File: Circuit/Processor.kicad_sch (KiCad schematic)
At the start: 22 parts, among them J6 Conn_01x03_Pin, J7 Conn_01x02_Pin, J8 Conn_01x02_Pin, U1 STM32G491CCUx, Y1 ECS-2520MV-xxx-xx

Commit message: Output job, Revision Box and reorganise
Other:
- company: Harry and Yuki - EEE3 Instrumentation -> Harry Hill and Yuki Hoshino
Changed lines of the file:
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@@
 	(title_block
 		(title "Processor")
-		(date "2026-03-02")
+		(date "2026-05-02")
 		(rev "1.0")
-		(company "Harry and Yuki - EEE3 Instrumentation")
+		(company "Harry Hill and Yuki Hoshino")
+		(comment 1 "LCR Meter")
 	)
 	(junction

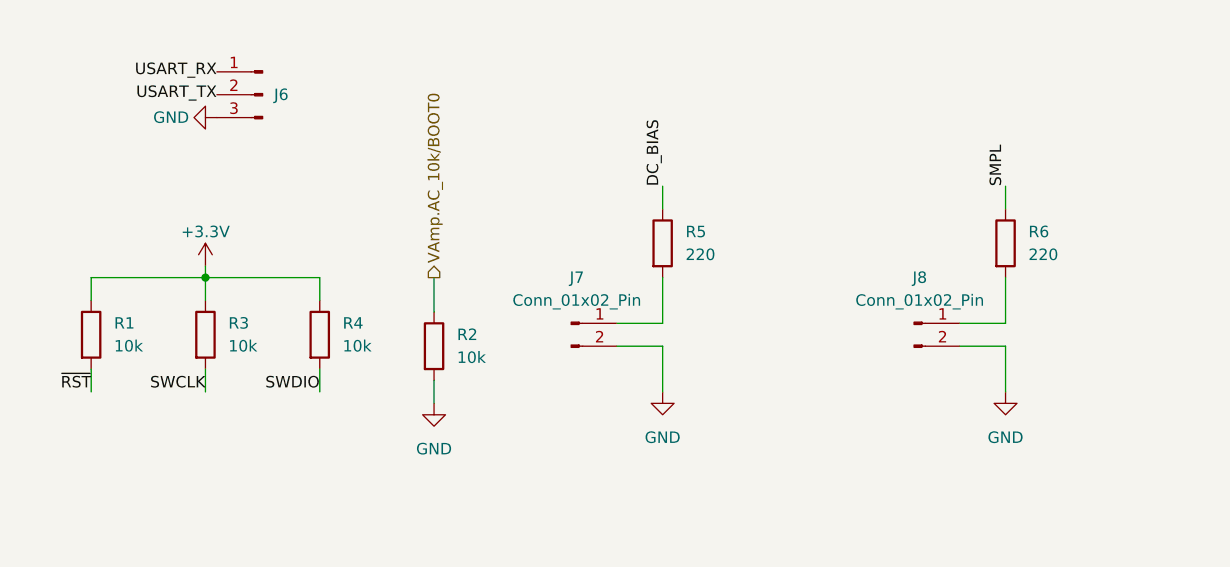
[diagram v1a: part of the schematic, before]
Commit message: Input Protection Second Attempt
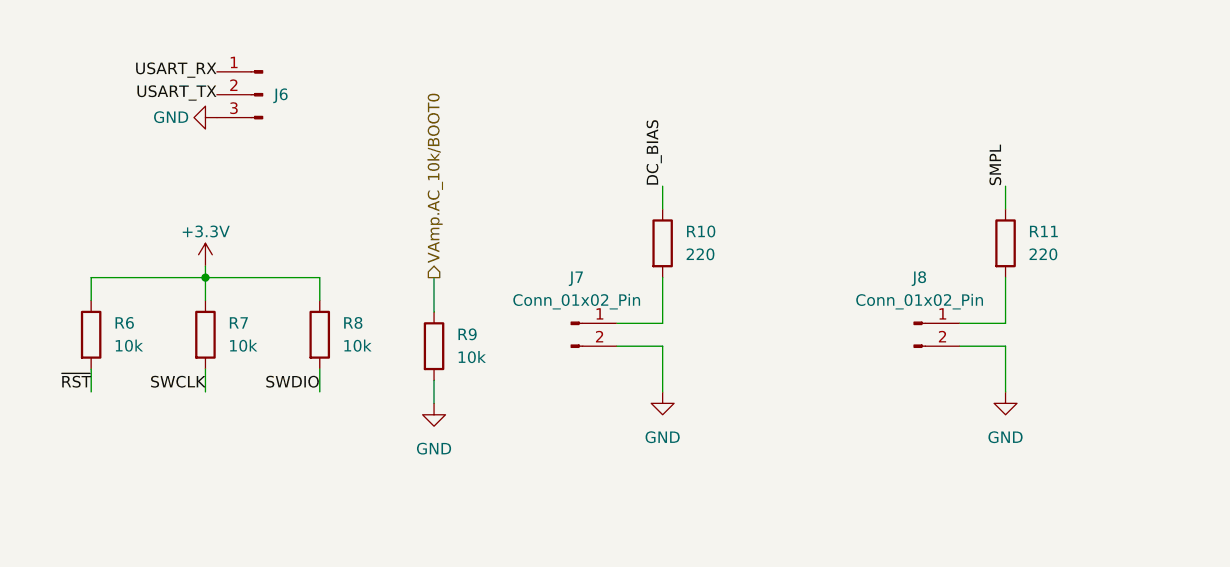
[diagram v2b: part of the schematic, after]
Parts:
- renumbered R5 to R10, R6 to R11, R1 to R6, R3 to R7, R4 to R8, R2 to R9

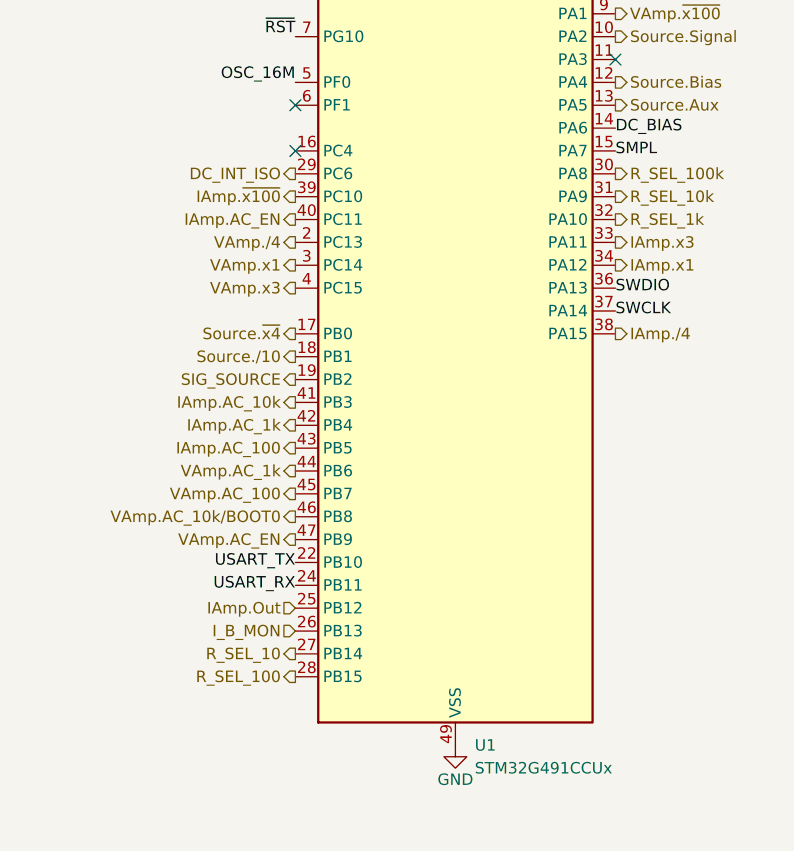
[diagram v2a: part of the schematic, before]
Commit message: New Resistor Selection Circuit
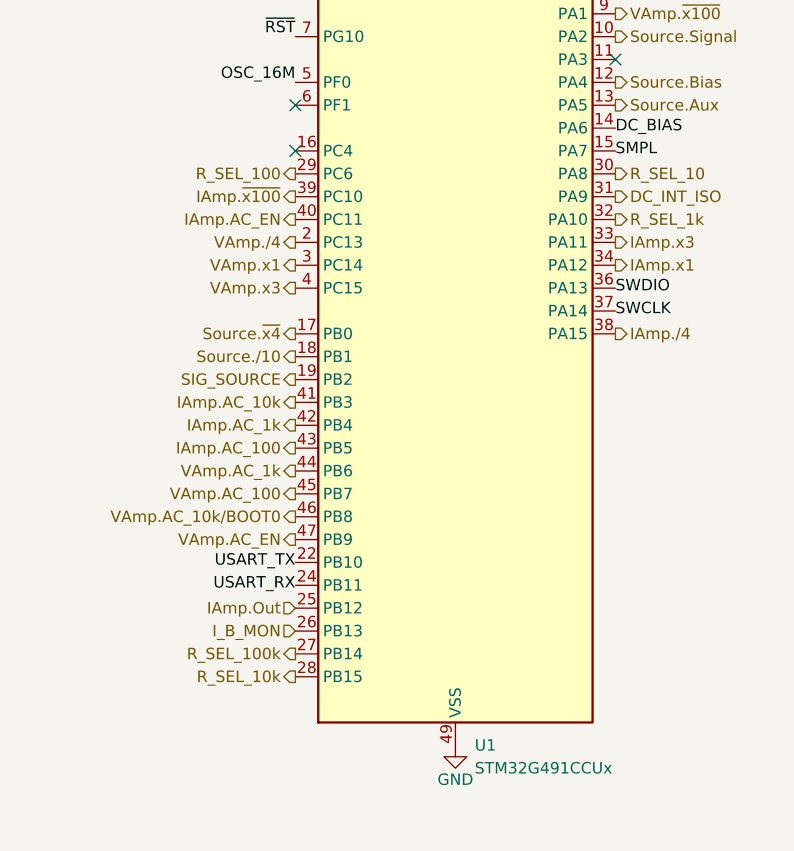
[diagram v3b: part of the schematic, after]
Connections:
- net DC_INT_ISO: now also U1.31 (PA9); no longer U1.29 (PC6)
- net R_SEL_10: now also U1.30 (PA8); no longer U1.27 (PB14)
- net R_SEL_100: now also U1.29 (PC6); no longer U1.28 (PB15)
- net R_SEL_100k: now also U1.27 (PB14); no longer U1.30 (PA8)
- net R_SEL_10k: now also U1.28 (PB15); no longer U1.31 (PA9)
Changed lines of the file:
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@@
 	(hierarchical_label "R_SEL_100"
 		(shape output)
-		(at 198.12 127 180)
+		(at 198.12 71.12 180)
 		(effects
 			(font
@@
 	(hierarchical_label "R_SEL_10k"
 		(shape output)
-		(at 233.68 73.66 0)
+		(at 198.12 127 180)
 		(effects
 			(font
 				(size 1.27 1.27)
 			)
-			(justify left)
+			(justify right)
 		)
 	)
@@
 	(hierarchical_label "R_SEL_10"
 		(shape output)
-		(at 198.12 124.46 180)
+		(at 233.68 71.12 0)
 		(effects
 			(font
 				(size 1.27 1.27)
 			)
-			(justify right)
+			(justify left)
 		)
 	)
@@
 	(hierarchical_label "R_SEL_100k"
 		(shape output)
-		(at 233.68 71.12 0)
+		(at 198.12 124.46 180)
 		(effects
 			(font
 				(size 1.27 1.27)
 			)
-			(justify left)
+			(justify right)
 		)
 	)
@@
 	(hierarchical_label "DC_INT_ISO"
 		(shape output)
-		(at 198.12 71.12 180)
+		(at 233.68 73.66 0)
 		(effects
 			(font
 				(size 1.27 1.27)
 			)
-			(justify right)
+			(justify left)
 		)
 	)
